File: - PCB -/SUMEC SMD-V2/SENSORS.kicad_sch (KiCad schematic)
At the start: 12 parts, among them J10 Conn_01x03_Pin, J3 Conn_01x04_Pin, J4 Conn_01x04_Pin, J9 Conn_01x03_Pin

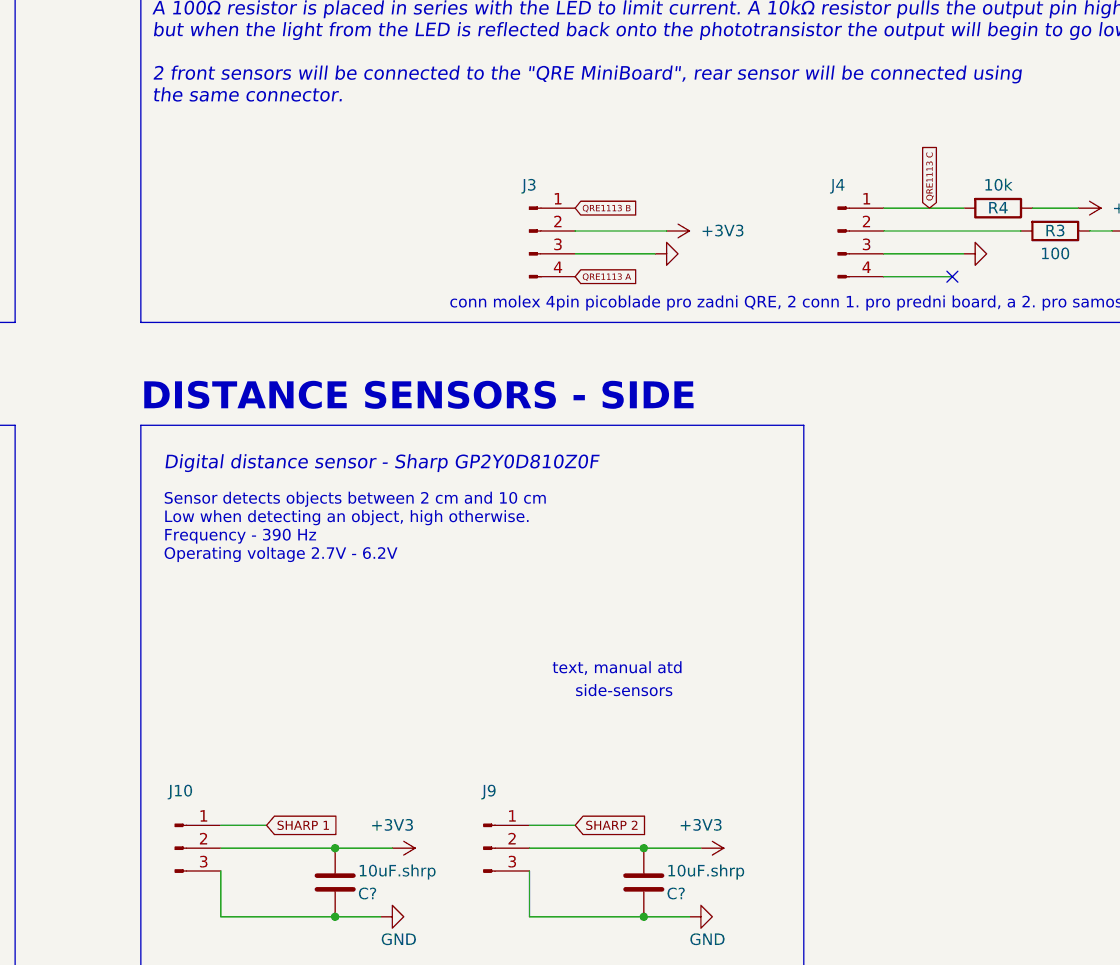
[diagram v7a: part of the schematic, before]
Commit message: 3d components models, footprint updates
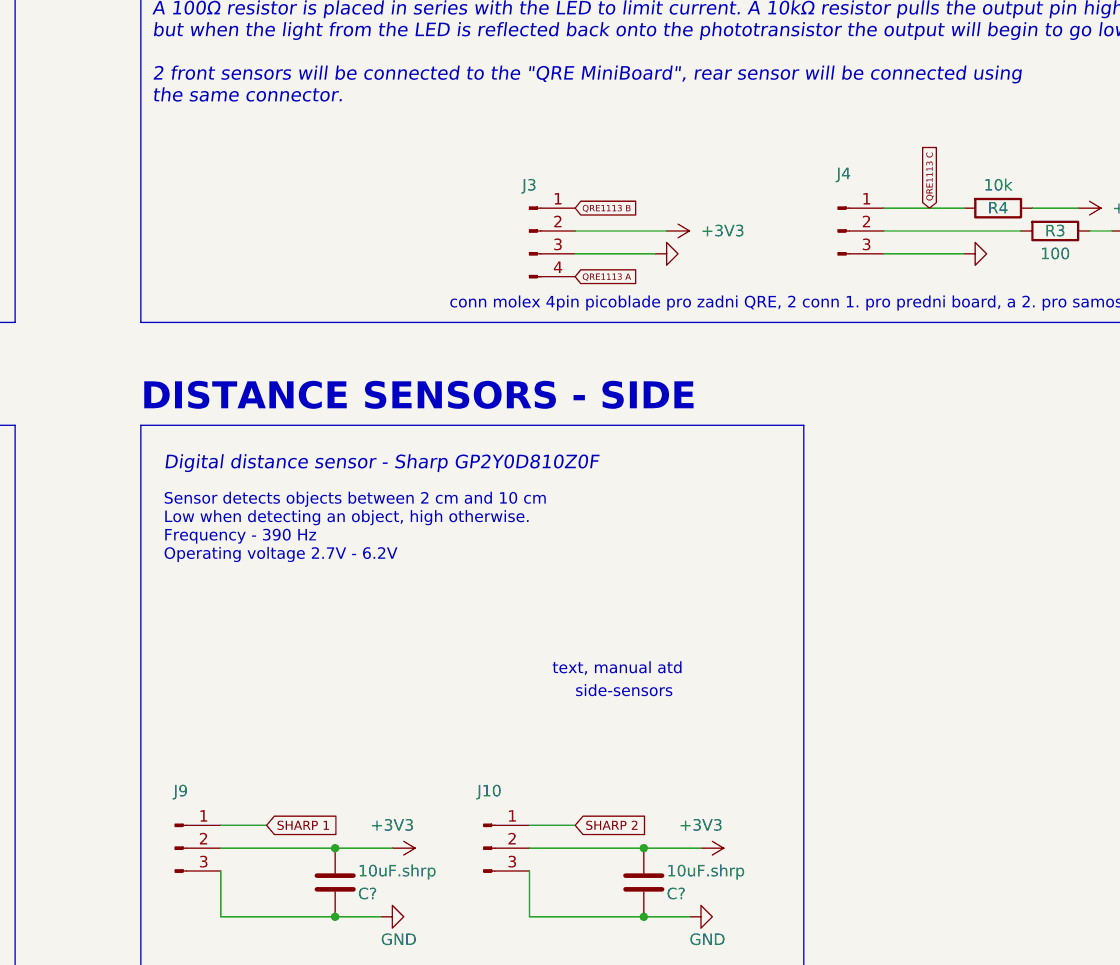
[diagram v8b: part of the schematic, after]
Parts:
- removed J4: Conn_01x04_Pin, Connector_Molex:Molex_PicoBlade_53398-0471_1x04-1MP_P1.25mm_Vertical, symbol Connector:Conn_01x04_Pin
- added J4: Conn_01x03_Pin, Connector_Molex:Molex_PicoBlade_53398-0371_1x03-1MP_P1.25mm_Vertical, symbol Connector:Conn_01x03_Pin
- J10, J9: footprint Connector_JST:JST_XH_B3B-XH-A_1x03_P2.50mm_Vertical -> Connector_Molex:Molex_PicoBlade_53398-0371_1x03-1MP_P1.25mm_Vertical
- U?: footprint Connector_PinSocket_2.54mm:PinSocket_1x03_P2.54mm_Vertical -> sumec-smdV2_library:TSOP
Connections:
- net GND: now also J4.3 (Pin_3)
- net QRE1113 C: now also J4.1 (Pin_1)
- net SHARP 1: now also J9.1 (Pin_1); no longer J10.1 (Pin_1)
- net SHARP 2: now also J10.1 (Pin_1); no longer J9.1 (Pin_1)
- net at R3.2: now also J4.2 (Pin_2)
- no-connect marks 4 -> 3
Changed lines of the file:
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@@
   )
   (no_connect (at 90.17 128.27))
-  (no_connect (at 209.55 69.85))
   (no_connect (at 41.91 128.27))
   (no_connect (at 66.04 128.27))
@@
     (stroke (width 0) (type default))
   )
-  (wire (pts (xy 209.55 69.85) (xy 201.93 69.85))
-    (stroke (width 0) (type default))
-  )
   (wire (pts (xy 68.58 130.81) (xy 66.04 130.81))
     (stroke (width 0) (type default))
@@
     )
   )
-  (symbol (lib_id "Connector:Conn_01x04_Pin") (at 196.85 64.77 0) (unit 1)
-    (in_bom yes) (on_board yes) (dnp no)
-    (property "Reference" "J4" (at 196.85 59.69 0)
-      (effects (font (size 1.27 1.27)))
-    )
-    (property "Value" "Conn_01x04_Pin" (at 197.485 60.96 0)
-      (effects (font (size 1.27 1.27)) hide)
-    )
-    (property "Footprint" "Connector_Molex:Molex_PicoBlade_53398-0471_1x04-1MP_P1.25mm_Vertical" (at 196.85 64.77 0)
-      (effects (font (size 1.27 1.27)) hide)
-    )
-    (property "Datasheet" "~" (at 196.85 64.77 0)
-      (effects (font (size 1.27 1.27)) hide)
-    )
-    (pin "1")
-    (pin "2")
-    (pin "3")
-    (pin "4")
-    (instances
-      (project "sumec"
-        (path "/fc70a1a8-ed7c-4a0f-9b1a-f23293528385/cfe10bc0-4e7a-493c-9fb6-0f9ed602f83c"
-          (reference "J4") (unit 1)
-        )
-      )
-    )
-  )
   (symbol (lib_id "Device:R") (at 214.63 62.23 270) (unit 1)
     (in_bom yes) (on_board yes) (dnp no)
@@
     )
   )
+  (symbol (lib_id "Connector:Conn_01x03_Pin") (at 157.48 133.35 0) (unit 1)
+    (in_bom yes) (on_board yes) (dnp no)
+    (property "Reference" "J10" (at 158.115 127 0)
+      (effects (font (size 1.27 1.27)))
+    )
+    (property "Value" "Conn_01x03_Pin" (at 158.75 138.43 0)
+      (effects (font (size 1.27 1.27)) hide)
+    )
+    (property "Footprint" "Connector_Molex:Molex_PicoBlade_53398-0371_1x03-1MP_P1.25mm_Vertical" (at 157.48 133.35 0)
+      (effects (font (size 1.27 1.27)) hide)
+    )
+    (property "Datasheet" "~" (at 157.48 133.35 0)
+      (effects (font (size 1.27 1.27)) hide)
+    )
+    (pin "1")
+    (pin "2")
+    (pin "3")
+    (instances
+      (project "sumec"
+        (path "/fc70a1a8-ed7c-4a0f-9b1a-f23293528385/cfe10bc0-4e7a-493c-9fb6-0f9ed602f83c"
+          (reference "J10") (unit 1)
+        )
+      )
+    )
+  )
   (symbol (lib_name "GND_1") (lib_id "power:GND") (at 176.53 67.31 90) (unit 1)
     (in_bom yes) (on_board yes) (dnp no) (fields_autoplaced)
@@
     )
   )
+  (symbol (lib_id "Connector:Conn_01x03_Pin") (at 123.19 133.35 0) (unit 1)
+    (in_bom yes) (on_board yes) (dnp no)
+    (property "Reference" "J9" (at 123.825 127 0)
+      (effects (font (size 1.27 1.27)))
+    )
+    (property "Value" "Conn_01x03_Pin" (at 124.46 138.43 0)
+      (effects (font (size 1.27 1.27)) hide)
+    )
+    (property "Footprint" "Connector_Molex:Molex_PicoBlade_53398-0371_1x03-1MP_P1.25mm_Vertical" (at 123.19 133.35 0)
+      (effects (font (size 1.27 1.27)) hide)
+    )
+    (property "Datasheet" "~" (at 123.19 133.35 0)
+      (effects (font (size 1.27 1.27)) hide)
+    )
+    (pin "1")
+    (pin "2")
+    (pin "3")
+    (instances
+      (project "sumec"
+        (path "/fc70a1a8-ed7c-4a0f-9b1a-f23293528385/cfe10bc0-4e7a-493c-9fb6-0f9ed602f83c"
+          (reference "J9") (unit 1)
+        )
+      )
+    )
+  )
   (symbol (lib_id "power:+3V3") (at 227.33 64.77 270) (unit 1)
     (in_bom yes) (on_board yes) (dnp no)
@@
     )
   )
+  (symbol (lib_id "Connector:Conn_01x03_Pin") (at 196.85 64.77 0) (unit 1)
+    (in_bom yes) (on_board yes) (dnp no)
+    (property "Reference" "J4" (at 197.485 58.42 0)
+      (effects (font (size 1.27 1.27)))
+    )
+    (property "Value" "Conn_01x03_Pin" (at 198.12 69.85 0)
+      (effects (font (size 1.27 1.27)) hide)
+    )
+    (property "Footprint" "Connector_Molex:Molex_PicoBlade_53398-0371_1x03-1MP_P1.25mm_Vertical" (at 196.85 64.77 0)
+      (effects (font (size 1.27 1.27)) hide)
+    )
+    (property "Datasheet" "~" (at 196.85 64.77 0)
+      (effects (font (size 1.27 1.27)) hide)
+    )
+    (pin "1")
+    (pin "2")
+    (pin "3")
+    (instances
+      (project "sumec"
+        (path "/fc70a1a8-ed7c-4a0f-9b1a-f23293528385/cfe10bc0-4e7a-493c-9fb6-0f9ed602f83c"
+          (reference "J4") (unit 1)
+        )
+      )
+    )
+  )
   (symbol (lib_id "power:+3V3") (at 177.8 64.77 270) (unit 1)
     (in_bom yes) (on_board yes) (dnp no)
@@
       (effects (font (size 1.27 1.27)) (justify right))
     )
-    (property "Footprint" "Connector_PinSocket_2.54mm:PinSocket_1x03_P2.54mm_Vertical" (at 52.07 69.215 0)
+    (property "Footprint" "sumec-smdV2_library:TSOP" (at 52.07 69.215 0)
       (effects (font (size 1.27 1.27)) hide)
     )
@@
     )
   )
-  (symbol (lib_id "Connector:Conn_01x03_Pin") (at 123.19 133.35 0) (unit 1)
-    (in_bom yes) (on_board yes) (dnp no)
-    (property "Reference" "J10" (at 123.825 127 0)
-      (effects (font (size 1.27 1.27)))
-    )
-    (property "Value" "Conn_01x03_Pin" (at 124.46 138.43 0)
-      (effects (font (size 1.27 1.27)) hide)
-    )
-    (property "Footprint" "Connector_JST:JST_XH_B3B-XH-A_1x03_P2.50mm_Vertical" (at 123.19 133.35 0)
-      (effects (font (size 1.27 1.27)) hide)
-    )
-    (property "Datasheet" "~" (at 123.19 133.35 0)
-      (effects (font (size 1.27 1.27)) hide)
-    )
-    (pin "1")
-    (pin "2")
-    (pin "3")
-    (instances
-      (project "sumec"
-        (path "/fc70a1a8-ed7c-4a0f-9b1a-f23293528385/cfe10bc0-4e7a-493c-9fb6-0f9ed602f83c"
-          (reference "J10") (unit 1)
-        )
-      )
-    )
-  )
   (symbol (lib_id "power:GND") (at 68.58 59.69 90) (unit 1)
     (in_bom yes) (on_board yes) (dnp no) (fields_autoplaced)
@@
         )
       )
-    )
-  )
-  (symbol (lib_id "Connector:Conn_01x03_Pin") (at 157.48 133.35 0) (unit 1)
-    (in_bom yes) (on_board yes) (dnp no)
-    (property "Reference" "J9" (at 158.115 127 0)
-      (effects (font (size 1.27 1.27)))
-    )
-    (property "Value" "Conn_01x03_Pin" (at 158.75 138.43 0)
-      (effects (font (size 1.27 1.27)) hide)
-    )
-    (property "Footprint" "Connector_JST:JST_XH_B3B-XH-A_1x03_P2.50mm_Vertical" (at 157.48 133.35 0)
-      (effects (font (size 1.27 1.27)) hide)
-    )
-    (property "Datasheet" "~" (at 157.48 133.35 0)
-      (effects (font (size 1.27 1.27)) hide)
-    )
-    (pin "1")
-    (pin "2")
-    (pin "3")
-    (instances
-      (project "sumec"
-        (path "/fc70a1a8-ed7c-4a0f-9b1a-f23293528385/cfe10bc0-4e7a-493c-9fb6-0f9ed602f83c"
-          (reference "J9") (unit 1)
-        )
-      )
